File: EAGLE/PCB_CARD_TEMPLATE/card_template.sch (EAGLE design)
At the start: 3 parts, among them M1 MOUNTING_3M_3.2MM, X1 CONN_SMD_67P-P0.5-V_NASB0-S67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, X2 M.2_MKEY_FINGERS

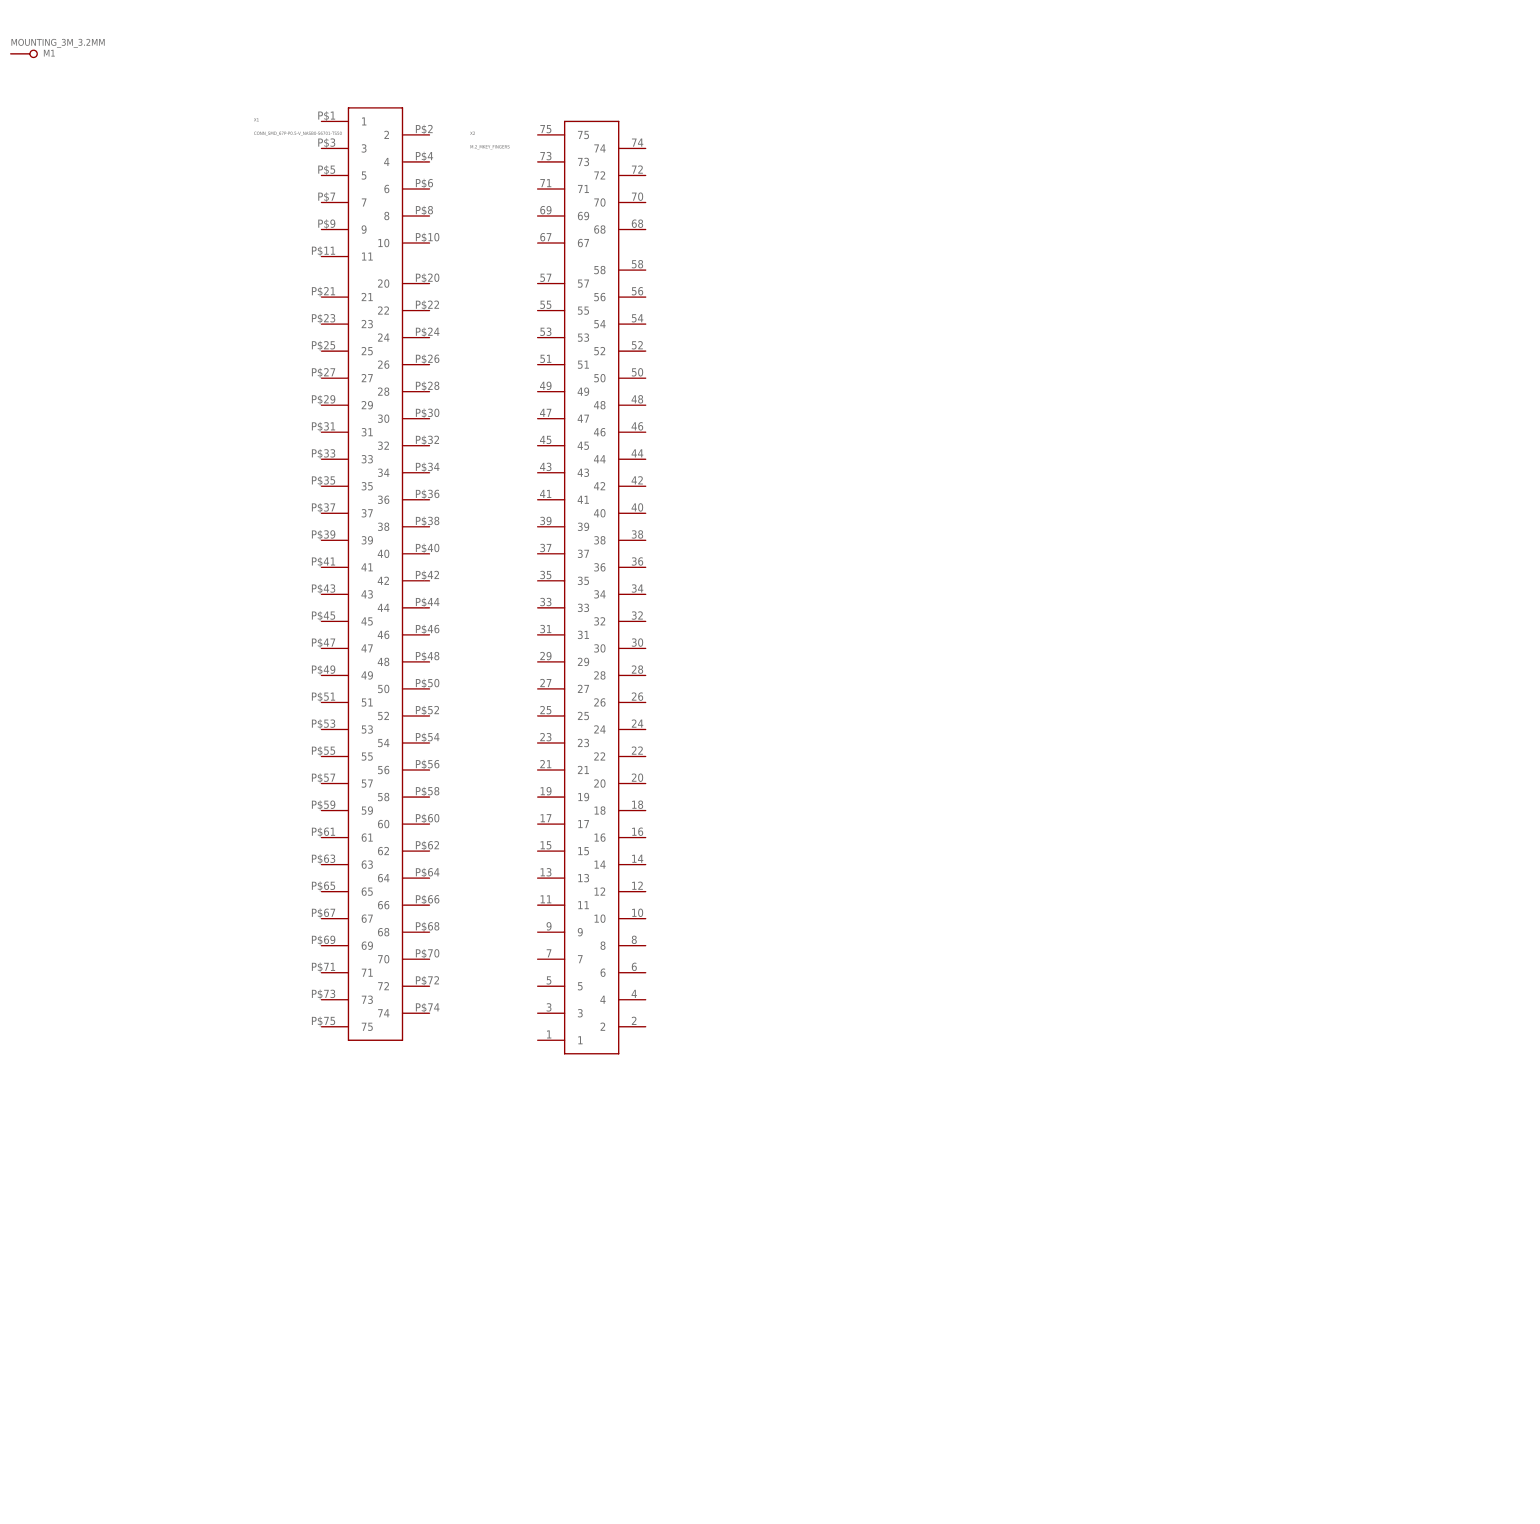
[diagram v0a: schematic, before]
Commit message: completed accessory card template
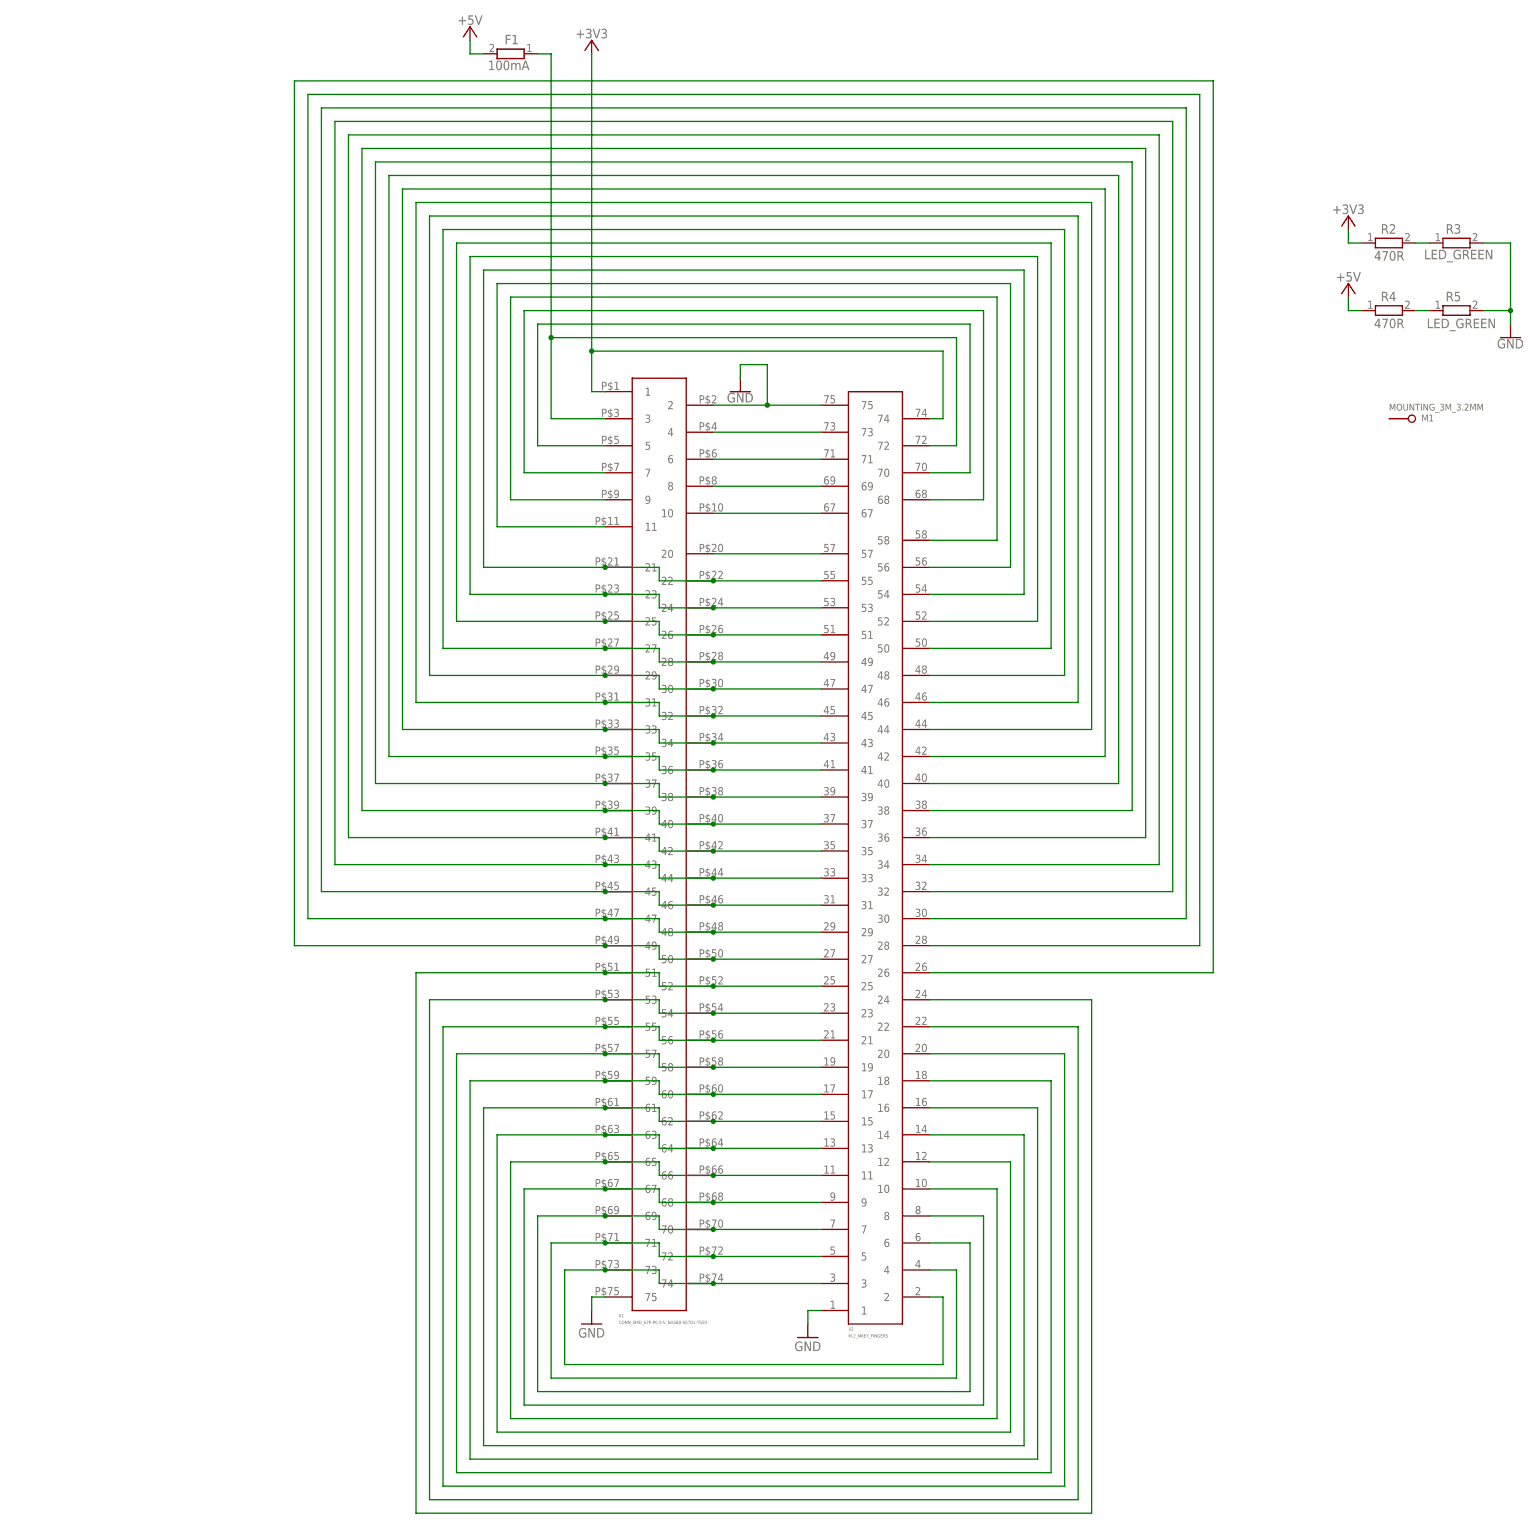
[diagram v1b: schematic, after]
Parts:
- added F1: 100mA, _NIBE_rcl:R-EU_R0805
- added R2, R4: 470R, _NIBE_rcl:R-EU_R0603
- added R3, R5: LED_GREEN, _NIBE_rcl:R-EU_R0603
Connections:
- new net +3V3: R2.1, X1.1, X2.74
- new net +5V: F1.2, R4.1
- new net GND: R3.2, R5.2, X1.2, X1.75, X2.1, X2.75
- new net N$1: X1.23, X1.24, X2.52, X2.53
- new net N$10: X1.59, X1.60, X2.16, X2.17
- new net N$11: X1.57, X1.58, X2.18, X2.19
- new net N$12: X1.55, X1.56, X2.20, X2.21
- new net N$13: X1.53, X1.54, X2.22, X2.23
- new net N$14: X1.51, X1.52, X2.24, X2.25
- new net N$15: X1.21, X1.22, X2.54, X2.55
- new net N$16: X1.27, X1.28, X2.48, X2.49
- new net N$17: X1.29, X1.30, X2.46, X2.47
- new net N$18: X1.31, X1.32, X2.44, X2.45
- new net N$19: X1.33, X1.34, X2.42, X2.43
- new net N$2: X1.25, X1.26, X2.50, X2.51
- new net N$20: X1.35, X1.36, X2.40, X2.41
- new net N$21: X1.37, X1.38, X2.38, X2.39
- new net N$22: X1.39, X1.40, X2.36, X2.37
- new net N$23: X1.41, X1.42, X2.34, X2.35
- new net N$24: X1.43, X1.44, X2.32, X2.33
- new net N$25: X1.45, X1.46, X2.30, X2.31
- new net N$26: X1.47, X1.48, X2.28, X2.29
- new net N$27: X1.49, X1.50, X2.26, X2.27
- new net N$28: X1.11, X2.56
- new net N$29: X1.9, X2.58
- new net N$3: X1.73, X1.74, X2.2, X2.3
- new net N$30: X1.7, X2.68
- new net N$31: X1.5, X2.70
- new net N$32: F1.1, X1.3, X2.72
- new net N$33: R2.2, R3.1
- new net N$35: X1.4, X2.73
- new net N$36: X1.6, X2.71
- new net N$37: X1.8, X2.69
- new net N$38: X1.10, X2.67
- new net N$39: X1.20, X2.57
- new net N$4: X1.71, X1.72, X2.4, X2.5
- new net N$40: R4.2, R5.1
- new net N$5: X1.69, X1.70, X2.6, X2.7
- new net N$6: X1.67, X1.68, X2.8, X2.9
- new net N$7: X1.65, X1.66, X2.10, X2.11
- new net N$8: X1.63, X1.64, X2.12, X2.13
- new net N$9: X1.61, X1.62, X2.14, X2.15
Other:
- moved on the sheet: M1, X1, X2

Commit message: pic24 card is done, gerbers and jlc files generated
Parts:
- removed F1: 100mA, _NIBE_rcl:R-EU_R0805
- removed R4: 470R, _NIBE_rcl:R-EU_R0603
- removed R5: LED_GREEN, _NIBE_rcl:R-EU_R0603
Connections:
- removed net N$32: F1.1, X1.3, X2.72
- removed net N$35: X1.4, X2.73
- removed net N$40: R4.2, R5.1
- net +5V: now also X1.3, X2.72; no longer F1.2, R4.1
- net GND: now also X1.4, X2.73; no longer R5.2
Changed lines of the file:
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@@
 <part name="GND3" library="supply" deviceset="GND" device=""/>
 <part name="+3V1" library="supply" deviceset="+3V3" device=""/>
-<part name="F1" library="_NIBE_rcl" deviceset="R-EU_" device="R0805" value="100mA"/>
 <part name="R2" library="_NIBE_rcl" deviceset="R-EU_" device="R0603" value="470R"/>
 <part name="R3" library="_NIBE_rcl" deviceset="R-EU_" device="R0603" value="LED_GREEN"/>
-<part name="R4" library="_NIBE_rcl" deviceset="R-EU_" device="R0603" value="470R"/>
-<part name="R5" library="_NIBE_rcl" deviceset="R-EU_" device="R0603" value="LED_GREEN"/>
 <part name="+5V1" library="supply" deviceset="+5V" device=""/>
 <part name="+3V2" library="supply" deviceset="+3V3" device=""/>
 <part name="GND4" library="supply" deviceset="GND" device=""/>
-<part name="+5V2" library="supply" deviceset="+5V" device=""/>
 </parts>
 <sheets>
@@
 <attribute name="VALUE" x="134.62" y="280.67" size="1.778" layer="96" rot="R180" align="center"/>
 </instance>
-<instance part="F1" gate="G$1" x="119.38" y="276.86" smashed="yes" rot="R180">
-<attribute name="NAME" x="120.904" y="280.4414" size="1.778" layer="95" rot="R180"/>
-<attribute name="VALUE" x="122.936" y="275.59" size="1.778" layer="96" rot="R180"/>
-</instance>
 <instance part="R2" gate="G$1" x="284.48" y="241.3" smashed="yes">
 <attribute name="NAME" x="282.956" y="243.0526" size="1.778" layer="95"/>
@@
 <attribute name="VALUE" x="291.084" y="238.252" size="1.778" layer="96"/>
 </instance>
-<instance part="R4" gate="G$1" x="284.48" y="228.6" smashed="yes">
-<attribute name="NAME" x="282.956" y="230.3526" size="1.778" layer="95"/>
-<attribute name="VALUE" x="281.686" y="225.298" size="1.778" layer="96"/>
-</instance>
-<instance part="R5" gate="G$1" x="297.18" y="228.6" smashed="yes">
-<attribute name="NAME" x="295.148" y="230.3526" size="1.778" layer="95"/>
-<attribute name="VALUE" x="291.592" y="225.298" size="1.778" layer="96"/>
-</instance>
-<instance part="+5V1" gate="A" x="111.76" y="279.4" smashed="yes">
-<attribute name="VALUE" x="111.76" y="283.21" size="1.778" layer="96" rot="R180" align="center"/>
+<instance part="+5V1" gate="A" x="127" y="276.86" smashed="yes">
+<attribute name="VALUE" x="127" y="280.67" size="1.778" layer="96" rot="R180" align="center"/>
 </instance>
 <instance part="+3V2" gate="G$1" x="276.86" y="243.84" smashed="yes">
 <attribute name="VALUE" x="276.86" y="247.65" size="1.778" layer="96" rot="R180" align="center"/>
 </instance>
-<instance part="GND4" gate="1" x="307.34" y="223.52" smashed="yes">
-<attribute name="VALUE" x="304.8" y="221.488" size="1.778" layer="96"/>
-</instance>
-<instance part="+5V2" gate="A" x="276.86" y="231.14" smashed="yes">
-<attribute name="VALUE" x="276.86" y="234.95" size="1.778" layer="96" rot="R180" align="center"/>
+<instance part="GND4" gate="1" x="307.34" y="233.68" smashed="yes">
+<attribute name="VALUE" x="304.8" y="231.648" size="1.778" layer="96"/>
 </instance>
 </instances>
@@
 <wire x1="167.64" y1="210.82" x2="167.64" y2="218.44" width="0.1524" layer="91"/>
 <junction x="167.64" y="210.82"/>
+<pinref part="X1" gate="G$1" pin="4"/>
+<pinref part="X2" gate="G$1" pin="73"/>
+<wire x1="157.48" y1="205.74" x2="167.64" y2="205.74" width="0.1524" layer="91"/>
+<wire x1="167.64" y1="205.74" x2="177.8" y2="205.74" width="0.1524" layer="91"/>
+<wire x1="167.64" y1="210.82" x2="167.64" y2="205.74" width="0.1524" layer="91"/>
+<junction x="167.64" y="205.74"/>
 </segment>
 <segment>
@@
 <pinref part="GND4" gate="1" pin="GND"/>
 <wire x1="302.26" y1="241.3" x2="307.34" y2="241.3" width="0.1524" layer="91"/>
-<wire x1="307.34" y1="241.3" x2="307.34" y2="228.6" width="0.1524" layer="91"/>
-<pinref part="R5" gate="G$1" pin="2"/>
-<wire x1="307.34" y1="228.6" x2="307.34" y2="226.06" width="0.1524" layer="91"/>
-<wire x1="302.26" y1="228.6" x2="307.34" y2="228.6" width="0.1524" layer="91"/>
-<junction x="307.34" y="228.6"/>
+<wire x1="307.34" y1="241.3" x2="307.34" y2="236.22" width="0.1524" layer="91"/>
 </segment>
 </net>
@@
 </segment>
 </net>
-<net name="N$32" class="0">
-<segment>
-<pinref part="X1" gate="G$1" pin="3"/>
-<wire x1="137.16" y1="208.28" x2="127" y2="208.28" width="0.1524" layer="91"/>
-<wire x1="127" y1="208.28" x2="127" y2="223.52" width="0.1524" layer="91"/>
-<wire x1="127" y1="223.52" x2="203.2" y2="223.52" width="0.1524" layer="91"/>
-<wire x1="203.2" y1="223.52" x2="203.2" y2="203.2" width="0.1524" layer="91"/>
-<pinref part="X2" gate="G$1" pin="72"/>
-<wire x1="203.2" y1="203.2" x2="198.12" y2="203.2" width="0.1524" layer="91"/>
-<wire x1="127" y1="223.52" x2="127" y2="276.86" width="0.1524" layer="91"/>
-<junction x="127" y="223.52"/>
-<pinref part="F1" gate="G$1" pin="1"/>
-<wire x1="127" y1="276.86" x2="124.46" y2="276.86" width="0.1524" layer="91"/>
-</segment>
-</net>
-<net name="N$35" class="0">
-<segment>
-<pinref part="X1" gate="G$1" pin="4"/>
-<pinref part="X2" gate="G$1" pin="73"/>
-<wire x1="157.48" y1="205.74" x2="177.8" y2="205.74" width="0.1524" layer="91"/>
-</segment>
-</net>
 <net name="N$36" class="0">
 <segment>
@@
 <net name="+5V" class="0">
 <segment>
-<pinref part="F1" gate="G$1" pin="2"/>
-<wire x1="114.3" y1="276.86" x2="111.76" y2="276.86" width="0.1524" layer="91"/>
-<wire x1="111.76" y1="276.86" x2="111.76" y2="279.4" width="0.1524" layer="91"/>
 <pinref part="+5V1" gate="A" pin="+5V"/>
-</segment>
-<segment>
-<pinref part="R4" gate="G$1" pin="1"/>
-<wire x1="279.4" y1="228.6" x2="276.86" y2="228.6" width="0.1524" layer="91"/>
-<pinref part="+5V2" gate="A" pin="+5V"/>
-<wire x1="276.86" y1="228.6" x2="276.86" y2="231.14" width="0.1524" layer="91"/>
+<pinref part="X1" gate="G$1" pin="3"/>
+<wire x1="137.16" y1="208.28" x2="127" y2="208.28" width="0.1524" layer="91"/>
+<wire x1="127" y1="208.28" x2="127" y2="223.52" width="0.1524" layer="91"/>
+<wire x1="127" y1="223.52" x2="203.2" y2="223.52" width="0.1524" layer="91"/>
+<wire x1="203.2" y1="223.52" x2="203.2" y2="203.2" width="0.1524" layer="91"/>
+<pinref part="X2" gate="G$1" pin="72"/>
+<wire x1="203.2" y1="203.2" x2="198.12" y2="203.2" width="0.1524" layer="91"/>
+<wire x1="127" y1="223.52" x2="127" y2="276.86" width="0.1524" layer="91"/>
+<junction x="127" y="223.52"/>
 </segment>
 </net>
@@
 </segment>
 </net>
-<net name="N$40" class="0">
-<segment>
-<pinref part="R5" gate="G$1" pin="1"/>
-<pinref part="R4" gate="G$1" pin="2"/>
-<wire x1="292.1" y1="228.6" x2="289.56" y2="228.6" width="0.1524" layer="91"/>
-</segment>
-</net>

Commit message: finish pwr supply card
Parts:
- renumbered R3 to LED1
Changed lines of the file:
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@@
 <part name="+3V1" library="supply" deviceset="+3V3" device=""/>
 <part name="R2" library="_NIBE_rcl" deviceset="R-EU_" device="R0603" value="470R"/>
-<part name="R3" library="_NIBE_rcl" deviceset="R-EU_" device="R0603" value="LED_GREEN"/>
+<part name="LED1" library="_NIBE_rcl" deviceset="R-EU_" device="R0603" value="LED_GREEN"/>
 <part name="+5V1" library="supply" deviceset="+5V" device=""/>
 <part name="+3V2" library="supply" deviceset="+3V3" device=""/>
@@
 <attribute name="VALUE" x="281.686" y="237.998" size="1.778" layer="96"/>
 </instance>
-<instance part="R3" gate="G$1" x="297.18" y="241.3" smashed="yes">
-<attribute name="NAME" x="295.148" y="243.0526" size="1.778" layer="95"/>
+<instance part="LED1" gate="G$1" x="297.18" y="241.3" smashed="yes">
+<attribute name="NAME" x="294.386" y="244.3226" size="1.778" layer="95"/>
 <attribute name="VALUE" x="291.084" y="238.252" size="1.778" layer="96"/>
 </instance>
@@
 </segment>
 <segment>
-<pinref part="R3" gate="G$1" pin="2"/>
+<pinref part="LED1" gate="G$1" pin="2"/>
 <pinref part="GND4" gate="1" pin="GND"/>
 <wire x1="302.26" y1="241.3" x2="307.34" y2="241.3" width="0.1524" layer="91"/>
@@
 <segment>
 <pinref part="R2" gate="G$1" pin="2"/>
-<pinref part="R3" gate="G$1" pin="1"/>
+<pinref part="LED1" gate="G$1" pin="1"/>
 <wire x1="289.56" y1="241.3" x2="292.1" y2="241.3" width="0.1524" layer="91"/>
 </segment>
